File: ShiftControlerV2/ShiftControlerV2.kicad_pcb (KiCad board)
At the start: 2 copper layers, 33 parts, among them J1 Conn_02x06_Counter_Clockwise, Q1 BTN8982TA, Q2 BTN8982TA, Q3 BSS138, Q4 BSS138, U1 ControllerBoardV2, U2 NCV7805BDTRKG

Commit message: Schematic Revised
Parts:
- removed C12, C13: 10n, Capacitor_SMD:C_0201_0603Metric_Pad0.64x0.40mm_HandSolder
- removed C14: 10u, Capacitor_SMD:C_0201_0603Metric_Pad0.64x0.40mm_HandSolder
- removed Q3, Q4: BSS138, digikey-footprints:SOT-23-3
- removed R10, R11, R12, R9: 10k, Resistor_SMD:R_0201_0603Metric_Pad0.64x0.40mm_HandSolder
- removed U2: NCV7805BDTRKG, Package_TO_SOT_SMD:TO-252-3_TabPin4
- C11: value 10u -> 1000u; footprint Capacitor_SMD:C_0201_0603Metric_Pad0.64x0.40mm_HandSolder -> Capacitor_THT:CP_Radial_D12.5mm_P5.00mm
- moved C5 50.0 mm to (100.3, 41.9)
- moved C10 49.3 mm to (115.6, 64.8), turned to 0 degrees
- moved Q2 45.4 mm to (106.4, 72.6), turned to 180 degrees
- moved C3 42.3 mm to (101.6, 57.1)
- moved C4 42.3 mm to (109.6, 59.7)
- moved Q1 42.3 mm to (110.8, 50.6)
- moved R3 42.3 mm to (97.4, 45.7)
- moved R1 42.3 mm to (97.8, 57.1)
- moved R2 42.3 mm to (97.8, 48.3)
- moved C1 42.3 mm to (97.8, 54.6)
- moved C2 42.3 mm to (94.0, 50.8)
- moved R4 42.3 mm to (94.0, 53.3)
- moved C8 39.8 mm to (118.1, 68.6), turned to 180 degrees
- moved C11 39.5 mm to (113.0, 91.4), turned to 0 degrees
- moved C9 35.9 mm to (108.4, 80.0), turned to 180 degrees
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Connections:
- net Net-(U1-Pad24) renamed CURRENT1
- net Net-(U1-Pad25) renamed CURRENT2
- J1 pad 7: Net-(J1-Pad7) -> UARTTX
- J1 pad 8: Net-(J1-Pad8) -> UARTRX
- R2 pad 2: +5V -> INH1
- R6 pad 2: +5V -> INH2
- U1 pad 17: Net-(U1-Pad17) -> CANL
- U1 pad 18: Net-(U1-Pad18) -> CANH
- U1 pad 22: Net-(U1-Pad22) -> UARTRX
- U1 pad 23: Net-(U1-Pad23) -> UARTTX
- U1 pad 28: Net-(U1-Pad28) -> INH2
- U1 pad 29: Net-(U1-Pad29) -> INH1

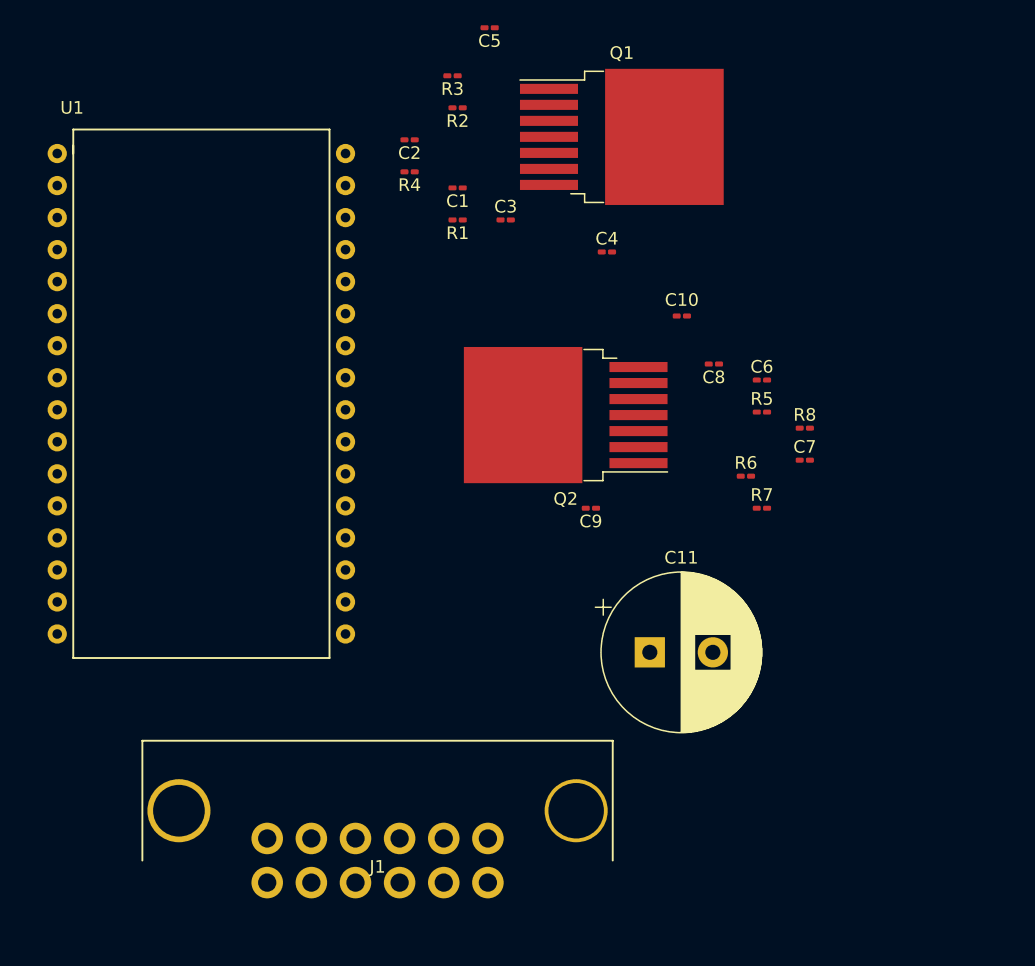
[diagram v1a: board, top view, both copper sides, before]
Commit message: PCB Revised, Con Added
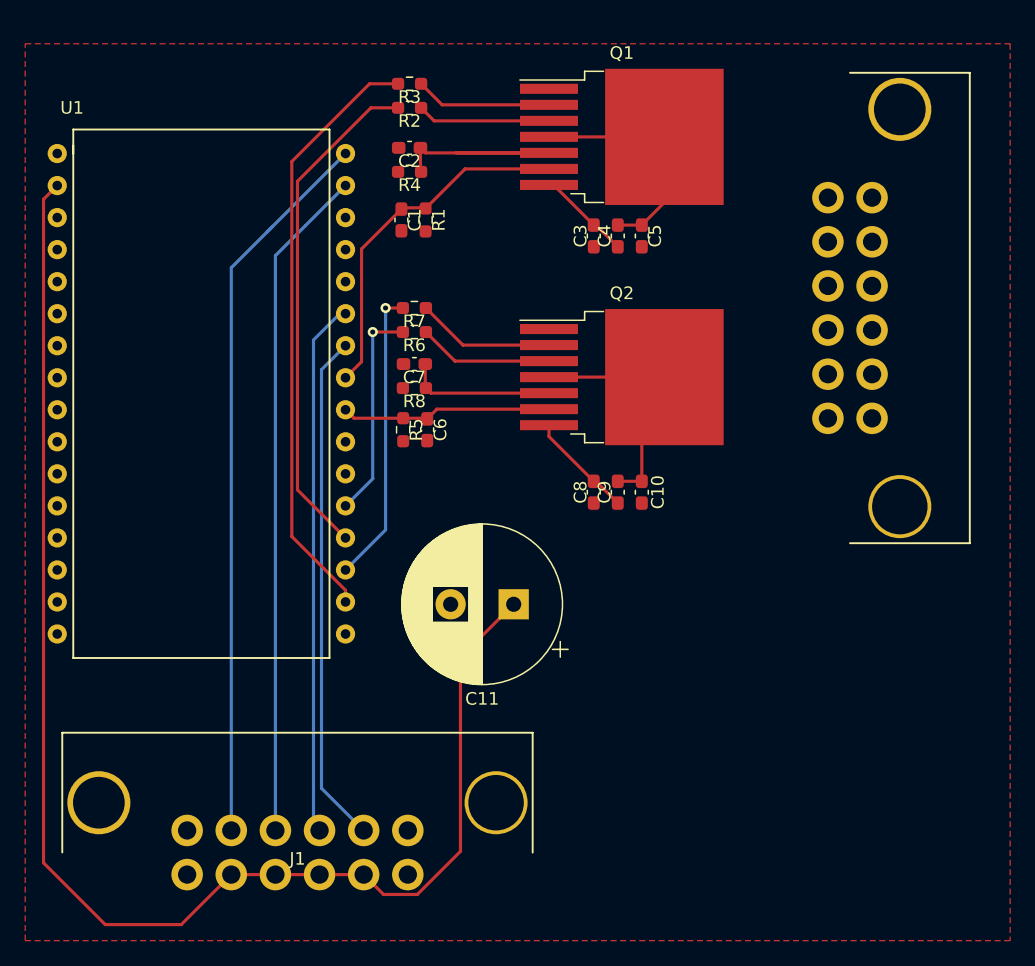
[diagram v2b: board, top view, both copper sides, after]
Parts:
- added J2: Conn_02x06_Counter_Clockwise, Lukas_Library:MX120G, F.Cu at (128.9, 64.1)
- C1, C10, C2, C3, C4, C5, C6, C7, C8, C9: footprint Capacitor_SMD:C_0201_0603Metric_Pad0.64x0.40mm_HandSolder -> Capacitor_SMD:C_0603_1608Metric_Pad1.08x0.95mm_HandSolder
- R1, R2, R3, R4, R5, R6, R7, R8: footprint Resistor_SMD:R_0201_0603Metric_Pad0.64x0.40mm_HandSolder -> Resistor_SMD:R_0603_1608Metric_Pad0.98x0.95mm_HandSolder
- moved C7 31.9 mm to (94.4, 68.6), turned to 180 degrees
- moved R7 31.8 mm to (94.4, 64.1), turned to 180 degrees
- moved R8 31.1 mm to (94.4, 70.5), turned to 180 degrees
- moved R6 28.7 mm to (94.4, 66.0), turned to 180 degrees
- moved R5 28.5 mm to (93.5, 73.8), turned to 270 degrees
- moved C6 26.8 mm to (95.4, 73.8), turned to 270 degrees
- moved C5 20.4 mm to (112.4, 58.4), turned to 270 degrees
- moved C10 14.3 mm to (112.4, 78.7), turned to 270 degrees
- moved C8 13.9 mm to (108.6, 78.7), turned to 90 degrees
- moved C11 11.4 mm to (102.2, 87.6), turned to 180 degrees
- moved C3 7.10 mm to (108.6, 58.4), turned to 90 degrees
- moved J1 6.38 mm to (85.1, 107.3)
- moved Q2 5.37 mm to (110.8, 69.6), turned to 0 degrees
- moved C1 5.13 mm to (93.3, 57.2), turned to 270 degrees
- moved R2 3.81 mm to (94.0, 48.3)
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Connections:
- C1 pad 1: Current1 -> CURRENT1
- C6 pad 1: Current2 -> CURRENT2
- J1 pad 1: +12V -> GND
- J1 pad 10: Net-(J1-Pad10) -> CANH
- J1 pad 12: CANH -> GND
- J1 pad 2: Net-(J1-Pad2) -> +12V
- J1 pad 3: Net-(J1-Pad3) -> +12V
- J1 pad 4: Net-(J1-Pad4) -> +12V
- J1 pad 5: Net-(J1-Pad5) -> +12V
- J1 pad 7: UARTTX -> GND
- J1 pad 8: UARTRX -> UARTTX
- J1 pad 9: Net-(J1-Pad9) -> UARTRX
- Q1 pad 6: Current1 -> CURRENT1
- Q2 pad 6: Current2 -> CURRENT2
- R1 pad 1: Current1 -> CURRENT1
- R5 pad 1: Current2 -> CURRENT2
- U1 pad 30: PB5 -> IN2
- U1 pad 31: PB4 -> IN1
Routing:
- net +12V: track 0.00 -> 130.7 mm
- net CANL: track 0.00 -> 58.0 mm
- net CANH: track 0.00 -> 53.4 mm
- net IN1: track 0.00 -> 47.7 mm
- net UARTRX: track 0.00 -> 43.2 mm
- net UARTTX: track 0.00 -> 40.6 mm
- net INH1: track 0.00 -> 40.2 mm
- net CURRENT1: track 0.00 -> 28.2 mm
- net IN2: track 0.00 -> 23.5 mm, vias 0 -> 1
- net OUT2: track 0.00 -> 20.1 mm
- net Net-(C2-Pad1): track 0.00 -> 19.7 mm
- net CURRENT2: track 0.00 -> 18.9 mm
- net OUT1: track 0.00 -> 18.8 mm
- net INH2: track 0.00 -> 17.1 mm, vias 0 -> 1
- net Net-(C7-Pad1): track 0.00 -> 11.9 mm
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- added copper zone on F.Cu, net GND

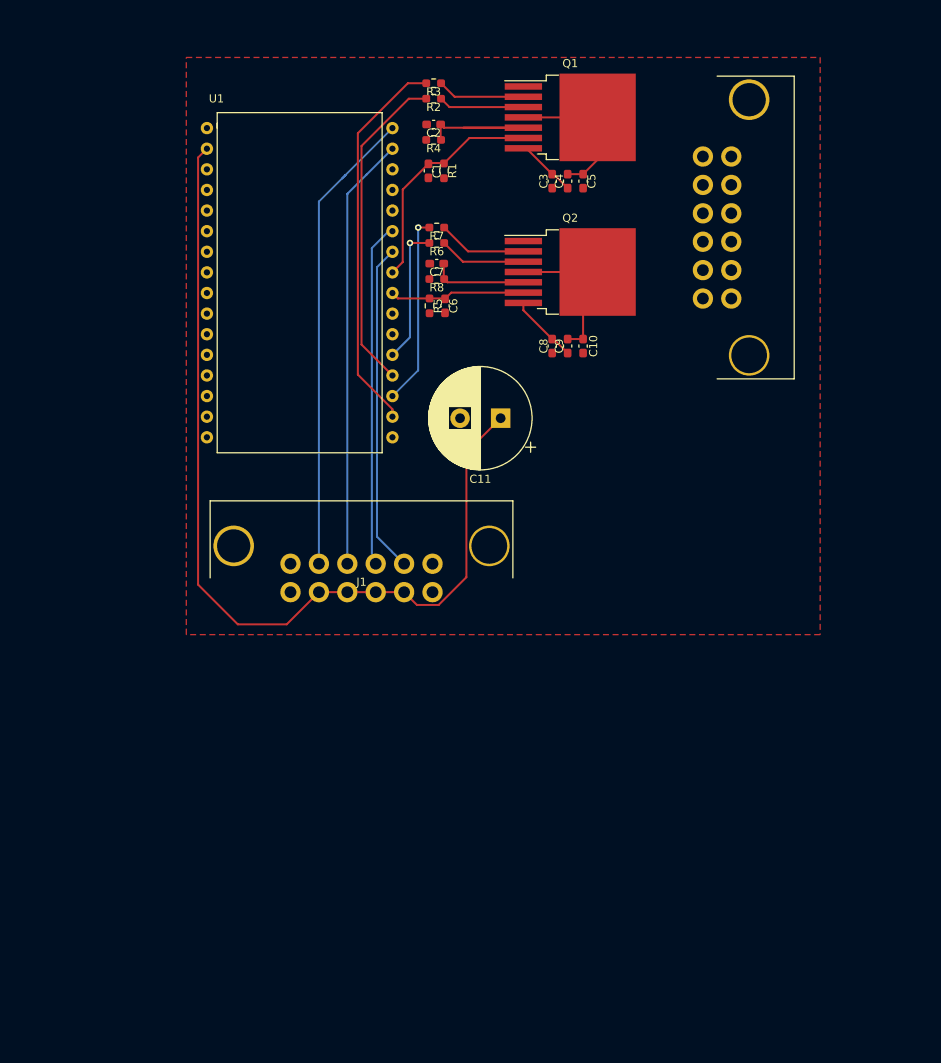
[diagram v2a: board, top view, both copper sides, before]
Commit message: Teeny tiny resistors
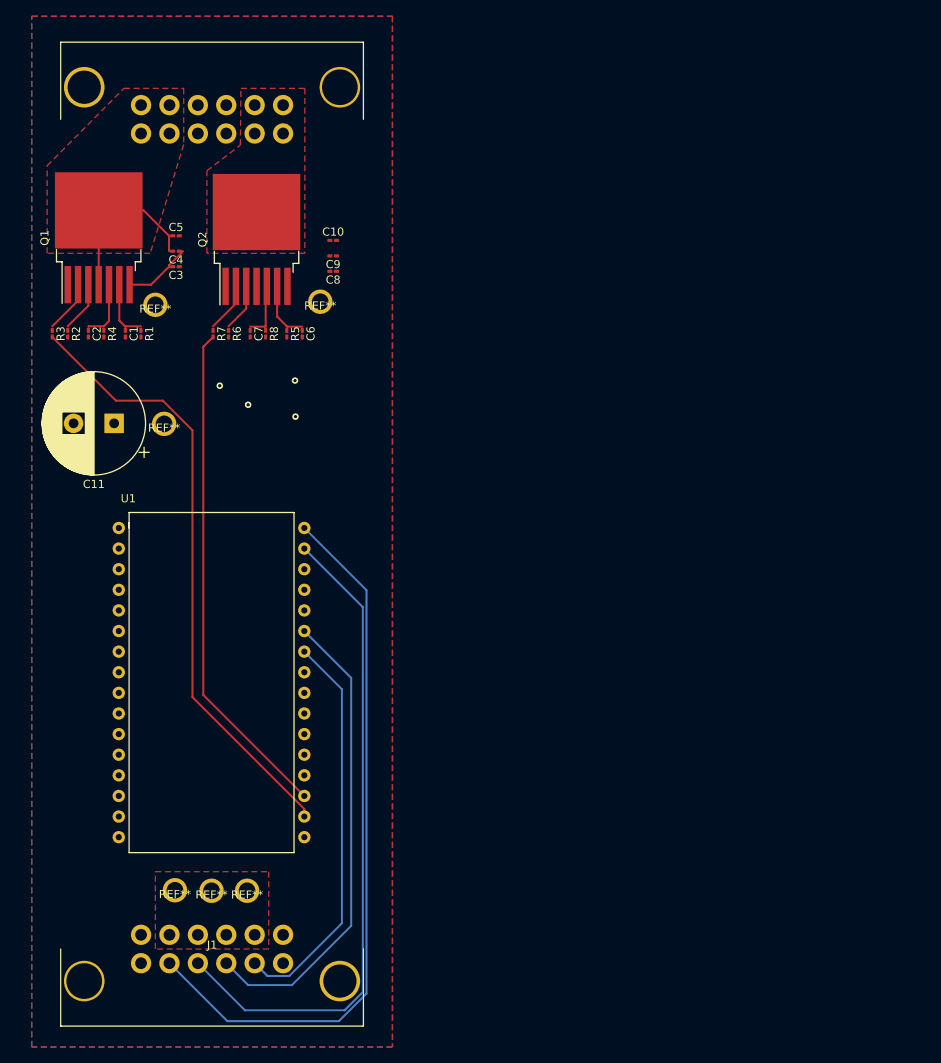
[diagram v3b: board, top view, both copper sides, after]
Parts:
- added REF**: 12_Gauge_TH, ShiftControlerFootprints:12_Gauge_TH, F.Cu at (71.0, 145.9)
- added REF**: 12_Gauge_TH, ShiftControlerFootprints:12_Gauge_TH, F.Cu at (66.6, 145.9)
- added REF**: 12_Gauge_TH, ShiftControlerFootprints:12_Gauge_TH, F.Cu at (80.0, 73.3)
- added REF**: 12_Gauge_TH, ShiftControlerFootprints:12_Gauge_TH, F.Cu at (60.8, 88.3)
- added REF**: 12_Gauge_TH, ShiftControlerFootprints:12_Gauge_TH, F.Cu at (62.1, 145.8)
- added REF**: 12_Gauge_TH, ShiftControlerFootprints:12_Gauge_TH, F.Cu at (59.7, 73.7)
- C1, C10, C2, C3, C4, C5, C6, C7, C8, C9: footprint Capacitor_SMD:C_0603_1608Metric_Pad1.08x0.95mm_HandSolder -> Capacitor_SMD:C_0201_0603Metric_Pad0.64x0.40mm_HandSolder
- R1, R2, R3, R4, R5, R6, R7, R8: footprint Resistor_SMD:R_0603_1608Metric_Pad0.98x0.95mm_HandSolder -> Resistor_SMD:R_0201_0603Metric_Pad0.64x0.40mm_HandSolder
- moved J2 63.6 mm to (66.7, 50.8), turned to 0 degrees
- moved Q1 60.0 mm to (52.7, 65.4), turned to 90 degrees
- moved R3 56.2 mm to (47.0, 77.2), turned to 270 degrees
- moved R2 53.6 mm to (48.9, 77.2), turned to 270 degrees
- moved C5 50.6 mm to (62.2, 65.2), turned to 0 degrees
- moved U1 50.5 mm to (55.2, 101.2)
- moved C2 49.7 mm to (51.4, 77.2), turned to 270 degrees
- moved J1 49.3 mm to (66.7, 153.0), turned to 180 degrees
- moved C4 49.0 mm to (62.2, 67.1), turned to 180 degrees
- moved C11 47.6 mm to (54.6, 88.3)
- moved C3 47.5 mm to (62.2, 69.0), turned to 180 degrees
- moved R4 47.1 mm to (53.3, 77.2), turned to 270 degrees
- moved C1 42.4 mm to (56.0, 77.2)
- moved R1 42.4 mm to (57.9, 77.2)
- moved Q2 38.9 mm to (72.2, 65.6), turned to 90 degrees
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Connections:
- J1 pad 10: CANH -> UARTRX
- J1 pad 11: CANL -> UARTTX
- J1 pad 8: UARTTX -> CANL
- J1 pad 9: UARTRX -> CANH
- U1 pad 24: CURRENT1 -> CURRENT2
- U1 pad 25: CURRENT2 -> CURRENT1
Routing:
- net +12V: track 130.7 -> 8.39 mm
- net INH1: track 40.2 -> 0.00 mm
- net IN2: track 23.5 -> 62.2 mm, vias 1 -> 0
- net CANL: track 58.0 -> 89.2 mm
- net CANH: track 53.4 -> 81.3 mm
- net IN1: track 47.7 -> 75.3 mm
- net CURRENT1: track 28.2 -> 7.42 mm, vias 0 -> 2
- net OUT2: track 20.1 -> 0.00 mm
- net INH2: track 17.1 -> 0.00 mm, vias 1 -> 0
- net UARTRX: track 43.2 -> 58.3 mm
- net Net-(C2-Pad1): track 19.7 -> 7.31 mm
- net CURRENT2: track 18.9 -> 7.34 mm, vias 0 -> 1
- net UARTTX: track 40.6 -> 49.5 mm
- net Net-(C7-Pad1): track 11.9 -> 6.91 mm
- net Net-(Q2-Pad2): track 11.0 -> 6.09 mm
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- added copper zone on F.Cu, net +12V
- added copper zone on B.Cu, net GND
- added copper zone on F.Cu, net OUT1
- added copper zone on F.Cu, net OUT2

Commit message: Rough Draft Finished
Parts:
- C1, C10, C2, C3, C4, C5, C6, C7, C8, C9: footprint Capacitor_SMD:C_0201_0603Metric_Pad0.64x0.40mm_HandSolder -> Capacitor_SMD:C_0603_1608Metric_Pad1.08x0.95mm_HandSolder
- R1, R2, R3, R4, R5, R6, R7, R8: footprint Resistor_SMD:R_0201_0603Metric_Pad0.64x0.40mm_HandSolder -> Resistor_SMD:R_0603_1608Metric_Pad0.98x0.95mm_HandSolder
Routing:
- net +12V: track 8.39 -> 81.0 mm
- net INH1: track 0.00 -> 72.3 mm, vias 0 -> 2
- net CURRENT1: track 7.42 -> 63.8 mm
- net INH2: track 0.00 -> 54.8 mm
- net CURRENT2: track 7.34 -> 50.9 mm, vias 1 -> 0
- net OUT2: track 0.00 -> 21.1 mm
- net GND: vias 1 -> 0

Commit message: First Review
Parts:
-  : renamed from REF** (x2)
- +12 V: renamed from REF** (x4)
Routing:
- net GND: track 0.00 -> 2.04 mm, vias 0 -> 6
- net IN1: track 75.3 -> 76.7 mm
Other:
- board text added: "Shift Controller Jan 2021 MB: Jacob Newman"

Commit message: Design reviewed
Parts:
- C11: footprint Capacitor_THT:CP_Radial_D12.5mm_P5.00mm -> Capacitor_THT:CP_Radial_D12.5mm_P7.50mm
- moved C10 13.0 mm to (68.6, 65.3)
- moved C8 13.0 mm to (68.6, 69.1)
- moved C9 13.0 mm to (68.6, 67.2)
- moved R5 7.20 mm to (83.1, 76.6)
- moved Q2 7.20 mm to (79.3, 65.0)
- moved C6 7.20 mm to (85.0, 76.6)
- moved C7 7.20 mm to (78.5, 76.6)
- moved R6 7.20 mm to (75.9, 76.6)
- moved R7 7.20 mm to (74.0, 76.6)
- moved R8 7.20 mm to (80.5, 76.6)
- moved +12 V 6.02 mm to (85.5, 70.7)
- moved +12 V 1.63 mm to (59.3, 72.1)
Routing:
- net OUT2: track 21.1 -> 15.0 mm
- net CURRENT2: track 50.9 -> 55.8 mm
- net INH2: track 54.8 -> 58.6 mm
- net IN2: track 62.2 -> 65.6 mm
- net +12V: track 81.0 -> 80.0 mm
- net GND: vias 6 -> 22
- added copper zone on B.Cu, net +12V

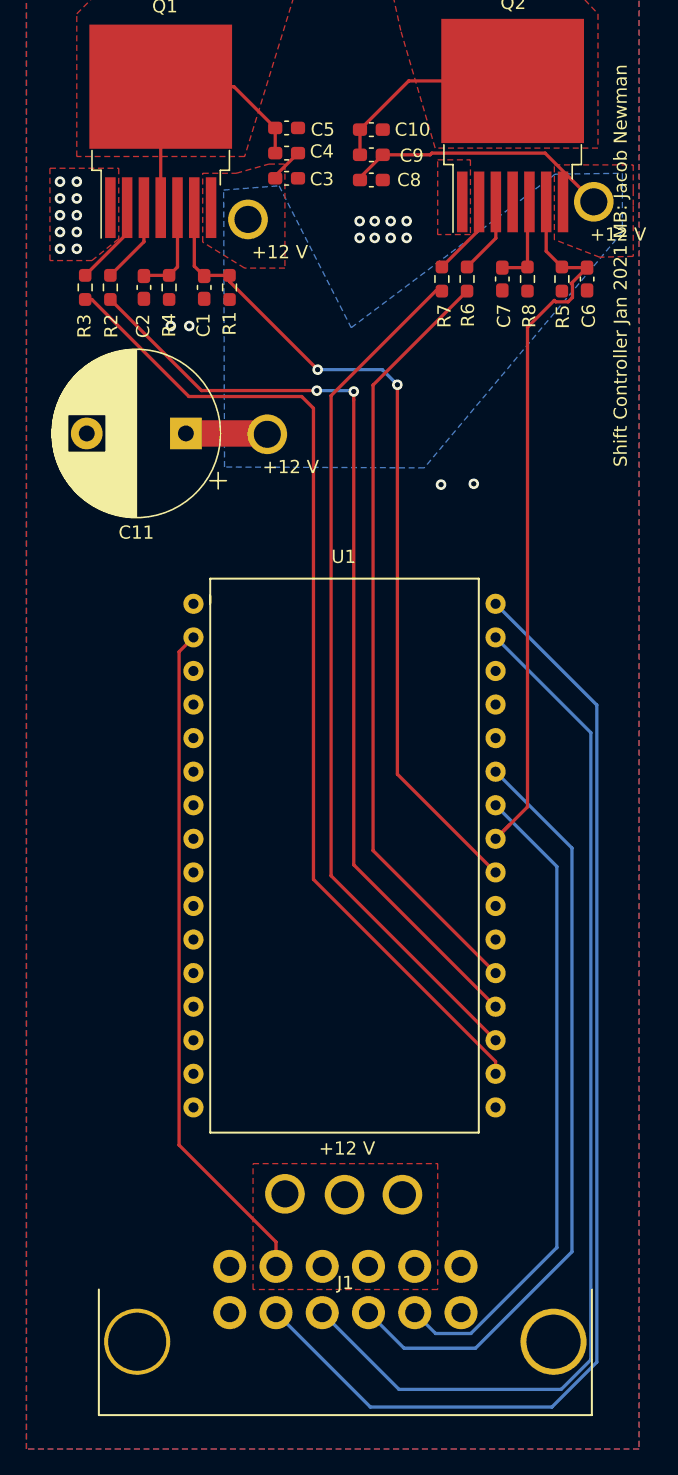
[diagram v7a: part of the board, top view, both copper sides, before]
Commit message: Update to provide additional power to micro
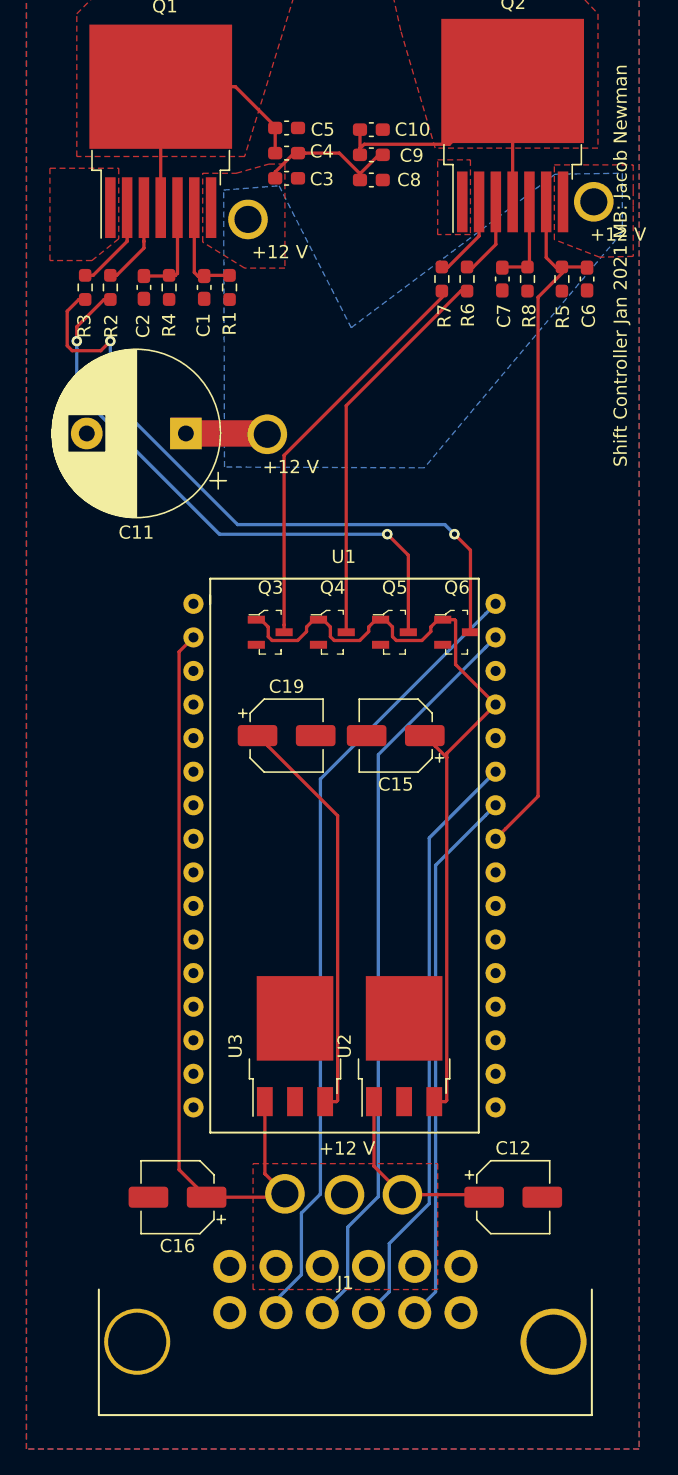
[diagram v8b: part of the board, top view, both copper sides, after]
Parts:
- added C12: 10u, Capacitor_SMD:CP_Elec_5x4.4, F.Cu at (79.4, 146.1)
- added C15: 10u, Capacitor_SMD:CP_Elec_5x4.4, F.Cu at (70.5, 111.1)
- added C16: 10u, Capacitor_SMD:CP_Elec_5x4.4, F.Cu at (54.0, 146.1)
- added C19: 10u, Capacitor_SMD:CP_Elec_5x4.4, F.Cu at (62.2, 111.1)
- added Q3: BSS138, digikey-footprints:SOT-23-3, F.Cu at (61.0, 103.3)
- added Q4: BSS138, digikey-footprints:SOT-23-3, F.Cu at (65.7, 103.3)
- added Q5: BSS138, digikey-footprints:SOT-23-3, F.Cu at (70.4, 103.3)
- added Q6: BSS138, digikey-footprints:SOT-23-3, F.Cu at (75.1, 103.3)
- added U2: LM1117-3.3, Package_TO_SOT_SMD:TO-252-3_TabPin4, F.Cu at (71.1, 134.6)
- added U3: NCV7805BDTRKG, Package_TO_SOT_SMD:TO-252-3_TabPin4, F.Cu at (62.9, 134.6)
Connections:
- R2 pad 2: INH1 -> INH1H
- R3 pad 2: IN1 -> IN1H
- R6 pad 2: INH2 -> INH2H
- R7 pad 2: IN2 -> IN2H
- U1 pad 28: INH2 -> INH2L
- U1 pad 29: INH1 -> INH1L
- U1 pad 30: IN2 -> IN2L
- U1 pad 31: IN1 -> IN1L
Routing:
- net IN1: track 76.7 -> 0.00 mm
- net INH1: track 72.3 -> 0.00 mm, vias 2 -> 0
- net IN2: track 65.6 -> 0.00 mm
- net +3V3: track 0.00 -> 63.3 mm
- net INH2: track 58.6 -> 0.00 mm
- net CURRENT1: track 63.8 -> 7.70 mm, vias 2 -> 0
- net IN1H: track 0.00 -> 50.6 mm, vias 0 -> 2
- net INH1H: track 0.00 -> 44.3 mm, vias 0 -> 2
- net +5V: track 0.00 -> 31.1 mm
- net IN2H: track 0.00 -> 30.8 mm
- net INH2H: track 0.00 -> 29.9 mm
- net CANL: track 89.2 -> 60.5 mm
- net CANH: track 81.3 -> 56.5 mm
- net UARTRX: track 58.3 -> 44.9 mm
- net OUT2: track 15.0 -> 25.2 mm
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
